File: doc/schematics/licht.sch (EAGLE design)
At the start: 16 parts, among them Q1 MOSFET-NCHANNELFDS6630A, X1 MKDSN1,5/2-5,08, X2 MKDSN1,5/2-5,08, X3 MKDSN1,5/2-5,08, X4 MKDSN1,5/2-5,08

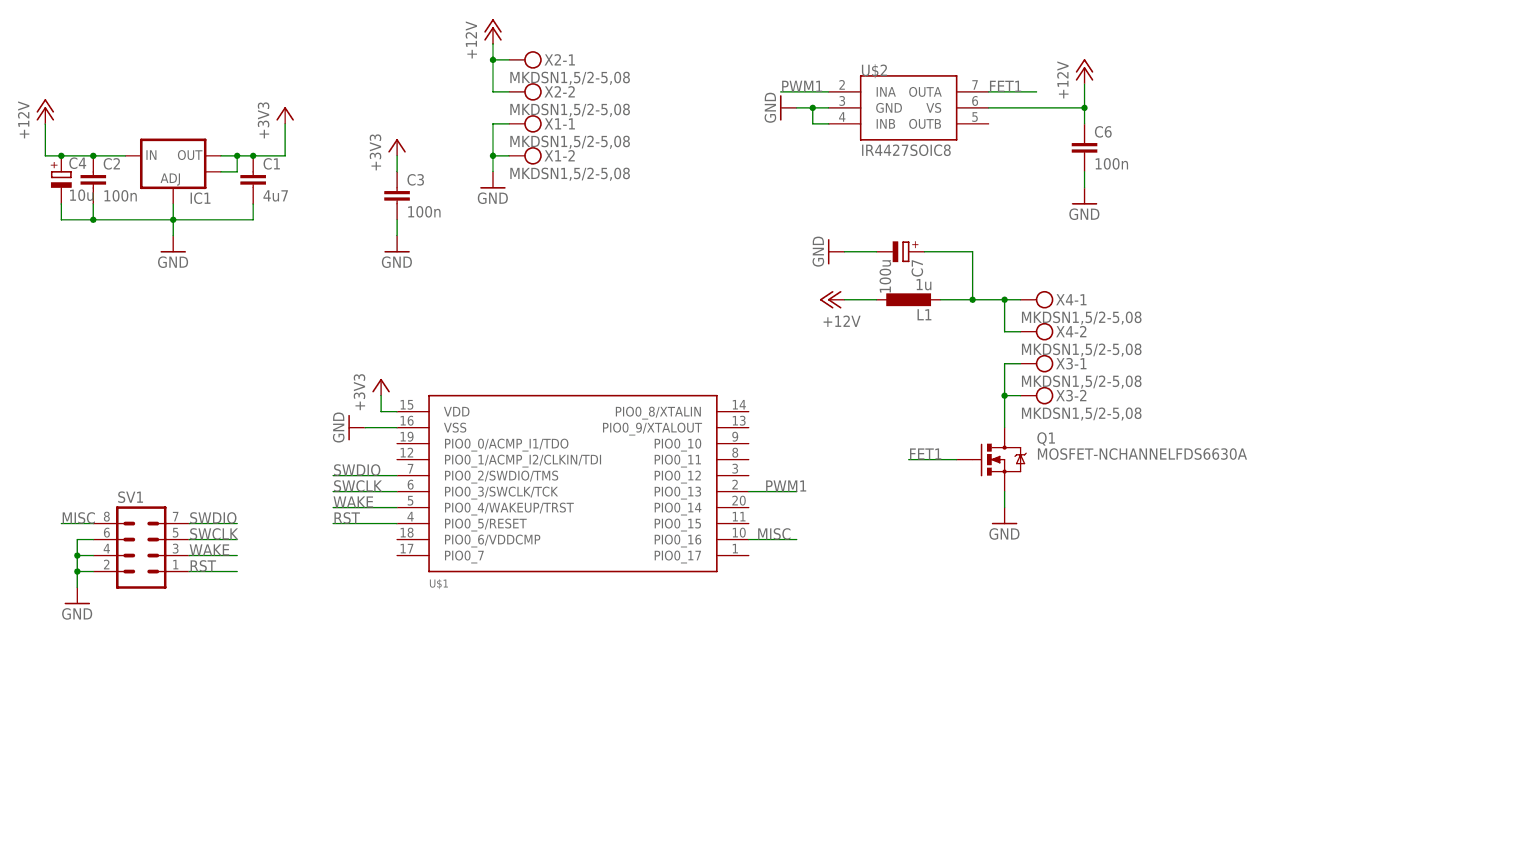
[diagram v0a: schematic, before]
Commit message: Switched layout and board.
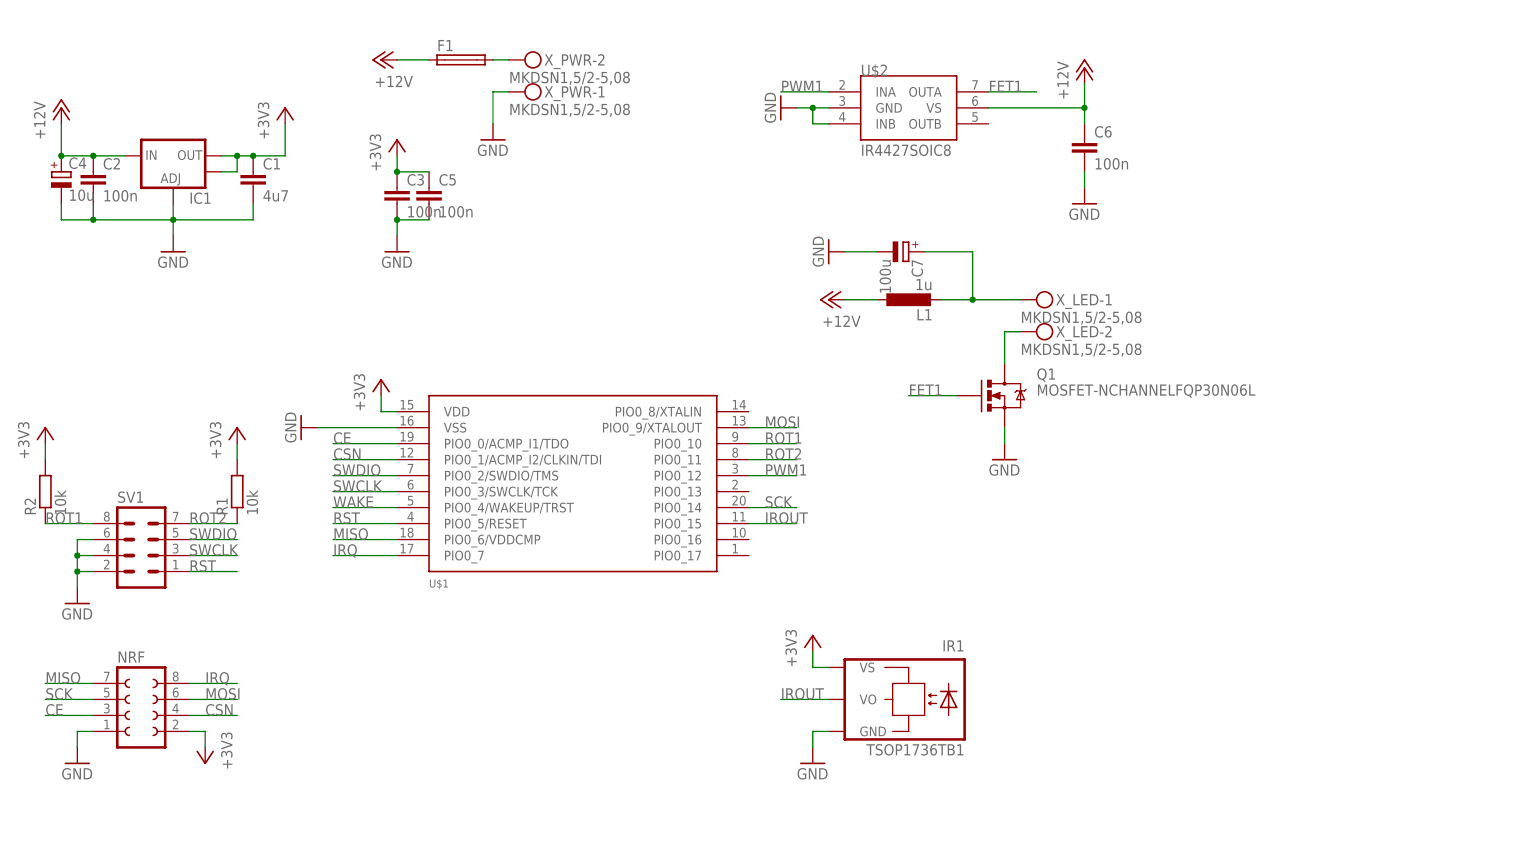
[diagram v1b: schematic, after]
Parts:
- removed X1, X2, X3: MKDSN1,5/2-5,08, con-phoenix-508:MKDSN1,5/2-5,08
- added C5: 100n, rcl:C-EUC0805
- added F1: (no value), fuse:SH22,5
- added IR1: TSOP1736TB1, tsop1736:TSOP1736TB1
- added NRF: (no value), florolf:FE04-2
- added R1, R2: 10k, rcl:R-EU_R0805
- added X_PWR: MKDSN1,5/2-5,08, con-phoenix-508:MKDSN1,5/2-5,08
- Q1: value MOSFET-NCHANNELFDS6630A -> MOSFET-NCHANNELFQP30N06L; device SparkFun-DiscreteSemi:MOSFET-NCHANNELFDS6630A -> SparkFun-DiscreteSemi:MOSFET-NCHANNELFQP30N06L
- renumbered X4 to X_LED
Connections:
- removed net MISC: SV1.8, U$1.PIO0_16
- removed net OUT: Q1.D, X3-1.KL, X3-2.KL
- new net CE: NRF.3, U$1.PIO0_0/ACMP_I1/TDO
- new net CSN: NRF.4, U$1.PIO0_1/ACMP_I2/CLKIN/TDI
- new net IROUT: IR1.VO, U$1.PIO0_15
- new net IRQ: NRF.8, U$1.PIO0_7
- new net MISO: NRF.7, U$1.PIO0_6/VDDCMP
- new net MOSI: NRF.6, U$1.PIO0_9/XTALOUT
- new net N$2: Q1.D, X_LED-2.KL
- new net N$3: F1.2, X_PWR-2.KL
- new net ROT1: R2.1, SV1.8, U$1.PIO0_10
- new net ROT2: R1.1, SV1.7, U$1.PIO0_11
- new net SCK: NRF.5, U$1.PIO0_14
- net +12V: now also F1.1; no longer X2-1.KL, X2-2.KL
- net +3V3: now also C5.1, IR1.VS, NRF.2, R1.2, R2.2
- net GND: now also C5.2, IR1.GND, NRF.1, X_PWR-1.KL; no longer X1-1.KL, X1-2.KL
- net N$1: no longer X_LED-2.KL
- net PWM1: now also U$1.PIO0_12; no longer U$1.PIO0_13
- net SWCLK: now also SV1.3; no longer SV1.5
- net SWDIO: now also SV1.5; no longer SV1.7
- net WAKE: no longer SV1.3
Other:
- moved on the sheet: Q1

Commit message: +Verpolungsschutz
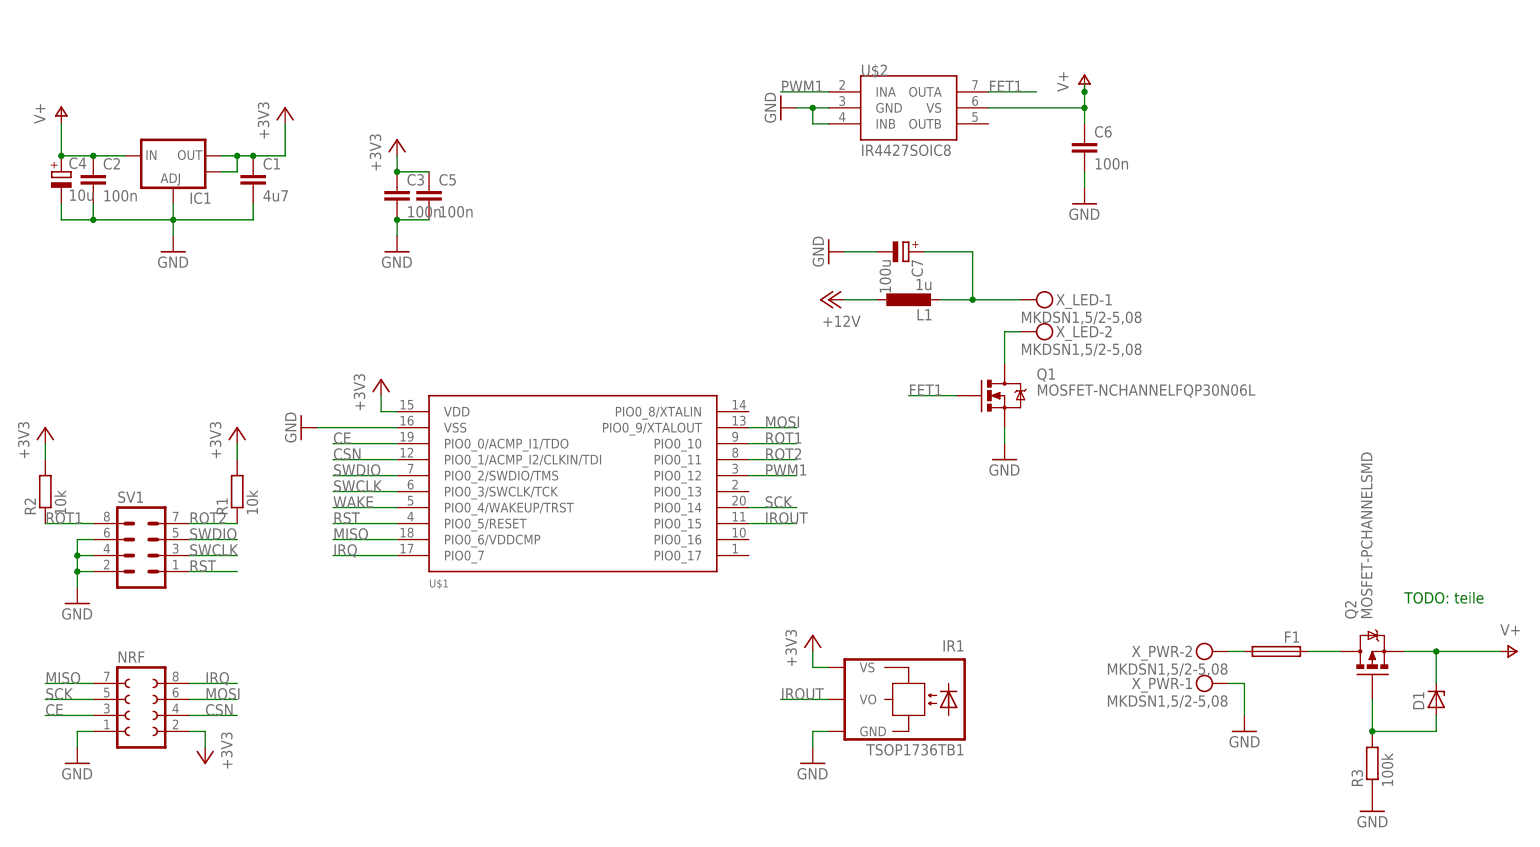
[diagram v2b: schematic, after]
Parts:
- added D1: (no value), diode:ZENER-DIODESOT223
- added Q2: MOSFET-PCHANNELSMD, SparkFun-DiscreteSemi:MOSFET-PCHANNELSMD
- added R3: 100k, rcl:R-EU_R0805
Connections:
- new net N$4: F1.1, Q2.D
- new net N$5: D1.A, Q2.G, R3.2
- new net V+: C2.1, C4.+, C6.1, D1.C, IC1.IN, Q2.S, U$2.VS
- net +12V: no longer C2.1, C4.+, C6.1, F1.1, IC1.IN, U$2.VS
- net GND: now also R3.1
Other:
- note added: "TODO: teile"
- moved on the sheet: F1, X_PWR-1, X_PWR-2
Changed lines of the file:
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@@
 <layer number="97" name="Info" color="7" fill="1" visible="yes" active="yes"/>
 <layer number="98" name="Guide" color="6" fill="1" visible="yes" active="yes"/>
+<layer number="99" name="SpiceOrder" color="5" fill="1" visible="yes" active="yes"/>
 <layer number="100" name="Muster" color="7" fill="1" visible="yes" active="yes"/>
 <layer number="101" name="Patch_Top" color="12" fill="4" visible="yes" active="yes"/>
@@
 <part name="U$1" library="LPC800" deviceset="LPC812M101JD20" device=""/>
 <part name="+3V1" library="supply1" deviceset="+3V3" device=""/>
-<part name="P+1" library="supply1" deviceset="+12V" device=""/>
 <part name="GND1" library="supply1" deviceset="GND" device=""/>
 <part name="IC1" library="SparkFun-PowerIC" deviceset="V_REG_LM1117" device="SOT223"/>
@@
 <part name="GND7" library="supply1" deviceset="GND" device=""/>
 <part name="X_PWR" library="con-phoenix-508" deviceset="MKDSN1,5/2-5,08" device=""/>
-<part name="P+3" library="supply1" deviceset="+12V" device=""/>
 <part name="SV1" library="con-lstb" deviceset="MA04-2" device=""/>
 <part name="Q1" library="SparkFun-DiscreteSemi" deviceset="MOSFET-NCHANNEL" device="FQP30N06L" value="MOSFET-NCHANNELFQP30N06L"/>
@@
 <part name="C2" library="rcl" deviceset="C-EU" device="C0805" value="100n"/>
 <part name="C4" library="rcl" deviceset="CPOL-EU" device="E2.5-6" value="10u"/>
-<part name="P+2" library="supply1" deviceset="+12V" device=""/>
 <part name="GND8" library="supply1" deviceset="GND" device=""/>
 <part name="P+4" library="supply1" deviceset="+12V" device=""/>
@@
 <part name="R2" library="rcl" deviceset="R-EU_" device="R0805" value="10k"/>
 <part name="F1" library="fuse" deviceset="SH22,5" device=""/>
+<part name="P+1" library="supply1" deviceset="V+" device=""/>
+<part name="P+2" library="supply1" deviceset="V+" device=""/>
+<part name="Q2" library="SparkFun-DiscreteSemi" deviceset="MOSFET-PCHANNEL" device="SMD"/>
+<part name="D1" library="diode" deviceset="ZENER-DIODE" device="SOT223"/>
+<part name="P+3" library="supply1" deviceset="V+" device=""/>
+<part name="R3" library="rcl" deviceset="R-EU_" device="R0805" value="100k"/>
+<part name="GND12" library="supply1" deviceset="GND" device=""/>
 </parts>
 <sheets>
 <sheet>
 <plain>
+<text x="203.2" y="40.64" size="1.778" layer="91">TODO: teile </text>
 </plain>
 <instances>
 <instance part="U$1" gate="G$1" x="71.12" y="58.42"/>
 <instance part="+3V1" gate="G$1" x="25.4" y="119.38"/>
-<instance part="P+1" gate="1" x="-10.16" y="119.38"/>
 <instance part="GND1" gate="1" x="7.62" y="96.52"/>
 <instance part="IC1" gate="G$1" x="7.62" y="111.76"/>
@@
 <instance part="GND5" gate="1" x="139.7" y="63.5"/>
 <instance part="GND6" gate="1" x="-7.62" y="40.64"/>
-<instance part="GND7" gate="1" x="58.42" y="114.3"/>
-<instance part="X_PWR" gate="-1" x="63.5" y="121.92"/>
-<instance part="X_PWR" gate="-2" x="63.5" y="127"/>
-<instance part="P+3" gate="1" x="40.64" y="127" rot="R90"/>
+<instance part="GND7" gate="1" x="177.8" y="20.32" rot="MR0"/>
+<instance part="X_PWR" gate="-1" x="172.72" y="27.94" rot="MR0"/>
+<instance part="X_PWR" gate="-2" x="172.72" y="33.02" rot="MR0"/>
 <instance part="SV1" gate="G$1" x="2.54" y="50.8"/>
 <instance part="Q1" gate="G$1" x="139.7" y="73.66"/>
@@
 <instance part="C2" gate="G$1" x="-5.08" y="109.22"/>
 <instance part="C4" gate="G$1" x="-10.16" y="109.22"/>
-<instance part="P+2" gate="1" x="152.4" y="125.73"/>
 <instance part="GND8" gate="1" x="104.14" y="119.38" rot="R270"/>
 <instance part="P+4" gate="1" x="111.76" y="88.9" rot="R90"/>
@@
 <instance part="R1" gate="G$1" x="17.78" y="58.42" rot="R90"/>
 <instance part="R2" gate="G$1" x="-12.7" y="58.42" rot="R90"/>
-<instance part="F1" gate="1" x="53.34" y="127"/>
+<instance part="F1" gate="1" x="182.88" y="33.02" rot="MR0"/>
+<instance part="P+1" gate="1" x="-10.16" y="119.38"/>
+<instance part="P+2" gate="1" x="152.4" y="124.46"/>
+<instance part="Q2" gate="G$1" x="198.12" y="33.02" rot="R90"/>
+<instance part="D1" gate="G$1" x="208.28" y="25.4" rot="R90"/>
+<instance part="P+3" gate="1" x="220.98" y="33.02" rot="R270"/>
+<instance part="R3" gate="G$1" x="198.12" y="15.24" rot="R90"/>
+<instance part="GND12" gate="1" x="198.12" y="7.62" rot="MR0"/>
 </instances>
 <busses>
@@
 <segment>
 <pinref part="GND7" gate="1" pin="GND"/>
-<wire x1="58.42" y1="121.92" x2="58.42" y2="116.84" width="0.1524" layer="91"/>
+<wire x1="177.8" y1="27.94" x2="177.8" y2="22.86" width="0.1524" layer="91"/>
 <pinref part="X_PWR" gate="-1" pin="KL"/>
-<wire x1="58.42" y1="121.92" x2="60.96" y2="121.92" width="0.1524" layer="91"/>
+<wire x1="177.8" y1="27.94" x2="175.26" y2="27.94" width="0.1524" layer="91"/>
+</segment>
+<segment>
+<pinref part="R3" gate="G$1" pin="1"/>
+<pinref part="GND12" gate="1" pin="GND"/>
 </segment>
 </net>
@@
 <pinref part="L1" gate="G$1" pin="1"/>
 </segment>
-<segment>
-<pinref part="U$2" gate="G$1" pin="VS"/>
-<pinref part="P+2" gate="1" pin="+12V"/>
-<wire x1="137.16" y1="119.38" x2="152.4" y2="119.38" width="0.1524" layer="91"/>
-<wire x1="152.4" y1="119.38" x2="152.4" y2="123.19" width="0.1524" layer="91"/>
-<pinref part="C6" gate="G$1" pin="1"/>
-<wire x1="152.4" y1="119.38" x2="152.4" y2="116.84" width="0.1524" layer="91"/>
-<junction x="152.4" y="119.38"/>
-</segment>
-<segment>
-<pinref part="IC1" gate="G$1" pin="IN"/>
-<wire x1="0" y1="111.76" x2="-5.08" y2="111.76" width="0.1524" layer="91"/>
-<wire x1="-5.08" y1="111.76" x2="-10.16" y2="111.76" width="0.1524" layer="91"/>
-<pinref part="C2" gate="G$1" pin="1"/>
-<junction x="-5.08" y="111.76"/>
-<pinref part="C4" gate="G$1" pin="+"/>
-<pinref part="P+1" gate="1" pin="+12V"/>
-<wire x1="-10.16" y1="116.84" x2="-10.16" y2="111.76" width="0.1524" layer="91"/>
-<junction x="-10.16" y="111.76"/>
-</segment>
-<segment>
-<pinref part="F1" gate="1" pin="1"/>
-<pinref part="P+3" gate="1" pin="+12V"/>
-<wire x1="43.18" y1="127" x2="48.26" y2="127" width="0.1524" layer="91"/>
-</segment>
 </net>
 <net name="FET1" class="0">
@@
 <pinref part="X_PWR" gate="-2" pin="KL"/>
 <pinref part="F1" gate="1" pin="2"/>
-<wire x1="58.42" y1="127" x2="60.96" y2="127" width="0.1524" layer="91"/>
-</segment>
-</net>
+<wire x1="177.8" y1="33.02" x2="175.26" y2="33.02" width="0.1524" layer="91"/>
+</segment>
+</net>
+<net name="N$4" class="0">
+<segment>
+<pinref part="F1" gate="1" pin="1"/>
+<wire x1="193.04" y1="33.02" x2="187.96" y2="33.02" width="0.1524" layer="91"/>
+<pinref part="Q2" gate="G$1" pin="D"/>
+</segment>
+</net>
+<net name="V+" class="0">
+<segment>
+<pinref part="IC1" gate="G$1" pin="IN"/>
+<wire x1="0" y1="111.76" x2="-5.08" y2="111.76" width="0.1524" layer="91"/>
+<wire x1="-5.08" y1="111.76" x2="-10.16" y2="111.76" width="0.1524" layer="91"/>
+<pinref part="C2" gate="G$1" pin="1"/>
+<junction x="-5.08" y="111.76"/>
+<pinref part="C4" gate="G$1" pin="+"/>
+<wire x1="-10.16" y1="116.84" x2="-10.16" y2="111.76" width="0.1524" layer="91"/>
+<junction x="-10.16" y="111.76"/>
+<pinref part="P+1" gate="1" pin="V+"/>
+</segment>
+<segment>
+<pinref part="U$2" gate="G$1" pin="VS"/>
+<wire x1="137.16" y1="119.38" x2="152.4" y2="119.38" width="0.1524" layer="91"/>
+<wire x1="152.4" y1="119.38" x2="152.4" y2="121.92" width="0.1524" layer="91"/>
+<pinref part="C6" gate="G$1" pin="1"/>
+<wire x1="152.4" y1="121.92" x2="152.4" y2="123.19" width="0.1524" layer="91"/>
+<wire x1="152.4" y1="119.38" x2="152.4" y2="116.84" width="0.1524" layer="91"/>
+<junction x="152.4" y="119.38"/>
+<pinref part="P+2" gate="1" pin="V+"/>
+<junction x="152.4" y="121.92"/>
+</segment>
+<segment>
+<pinref part="Q2" gate="G$1" pin="S"/>
+<wire x1="203.2" y1="33.02" x2="208.28" y2="33.02" width="0.1524" layer="91"/>
+<pinref part="D1" gate="G$1" pin="C"/>
+<wire x1="208.28" y1="33.02" x2="218.44" y2="33.02" width="0.1524" layer="91"/>
+<wire x1="208.28" y1="27.94" x2="208.28" y2="33.02" width="0.1524" layer="91"/>
+<junction x="208.28" y="33.02"/>
+<pinref part="P+3" gate="1" pin="V+"/>
+</segment>
+</net>
+<net name="N$5" class="0">
+<segment>
+<pinref part="Q2" gate="G$1" pin="G"/>
+<wire x1="198.12" y1="25.4" x2="198.12" y2="20.32" width="0.1524" layer="91"/>
+<wire x1="198.12" y1="20.32" x2="208.28" y2="20.32" width="0.1524" layer="91"/>
+<pinref part="D1" gate="G$1" pin="A"/>
+<wire x1="208.28" y1="20.32" x2="208.28" y2="22.86" width="0.1524" layer="91"/>
+<pinref part="R3" gate="G$1" pin="2"/>
+<junction x="198.12" y="20.32"/>
+</segment>
+</net>

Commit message: pinheader geändert, reichelt-kompatiblen sicherungshalter
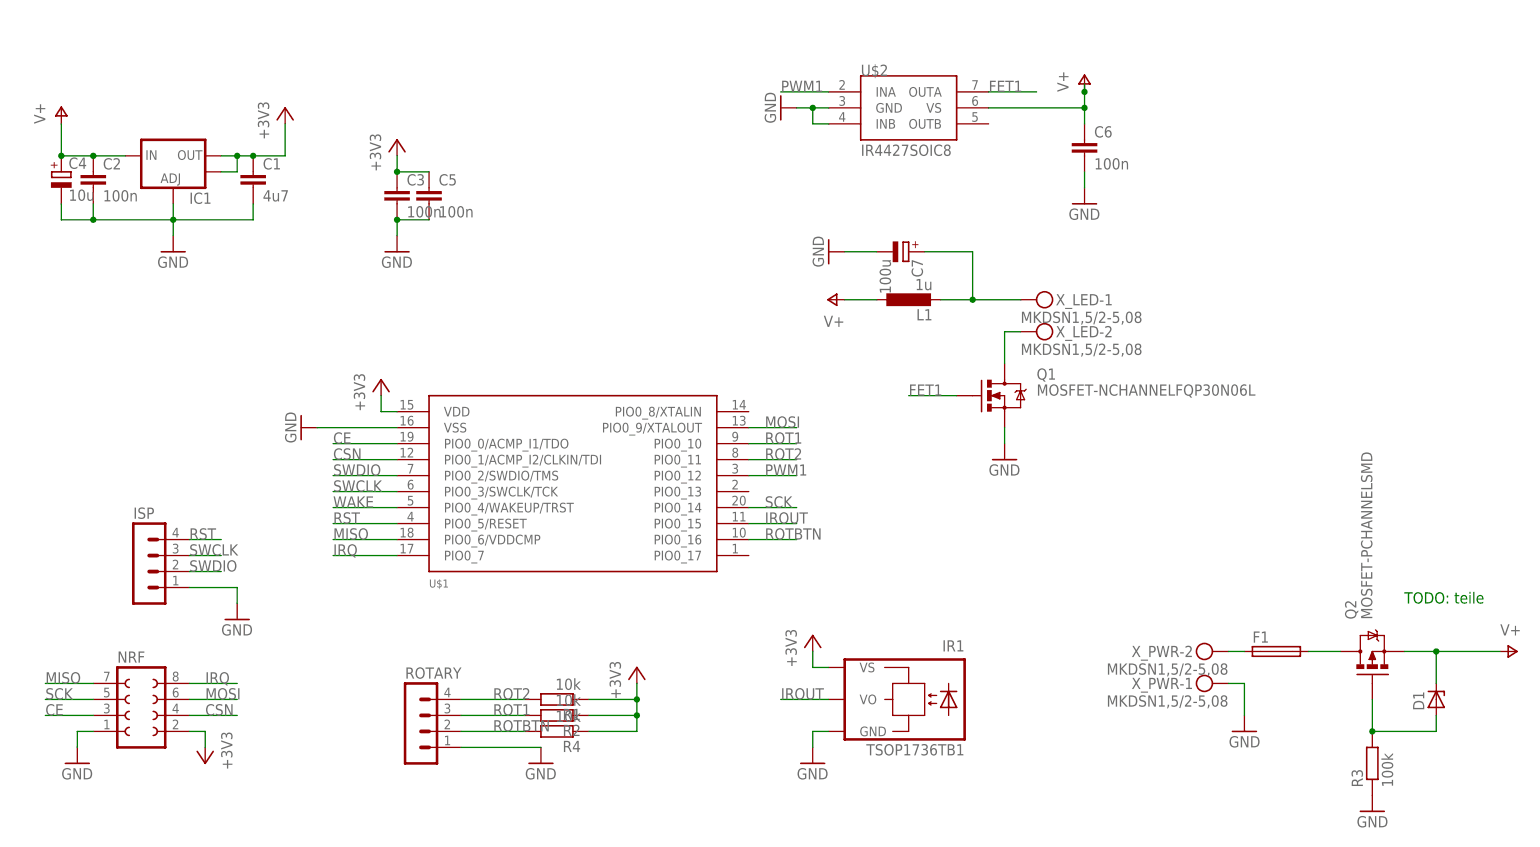
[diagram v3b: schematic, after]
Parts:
- removed SV1: (no value), con-lstb:MA04-2
- added ISP, ROTARY: (no value), con-lstb:MA04-1
- added R4: 10k, rcl:R-EU_R0805
- F1: device fuse:SH22,5 -> sprawl:PTF45
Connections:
- removed net +12V: L1.1
- new net ROTBTN: R4.2, ROTARY.2, U$1.PIO0_16
- net +3V3: now also R1.1, R2.1, R4.1; no longer R1.2, R2.2
- net GND: now also ISP.1, ROTARY.1; no longer SV1.2, SV1.4, SV1.6
- net N$3: now also F1.1; no longer F1.2
- net N$4: now also F1.2; no longer F1.1
- net ROT1: now also R2.2, ROTARY.3; no longer R2.1, SV1.8
- net ROT2: now also R1.2, ROTARY.4; no longer R1.1, SV1.7
- net RST: now also ISP.4; no longer SV1.1
- net SWCLK: now also ISP.3; no longer SV1.3
- net SWDIO: now also ISP.2; no longer SV1.5
- net V+: now also L1.1
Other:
- moved on the sheet: R1, R2
